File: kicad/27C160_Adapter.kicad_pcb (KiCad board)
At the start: 2 copper layers, 82.4 x 43.1 mm, 10 parts, among them Q1 BC327, SW1 MS22D16, SW2 DIP, U1 27C4002

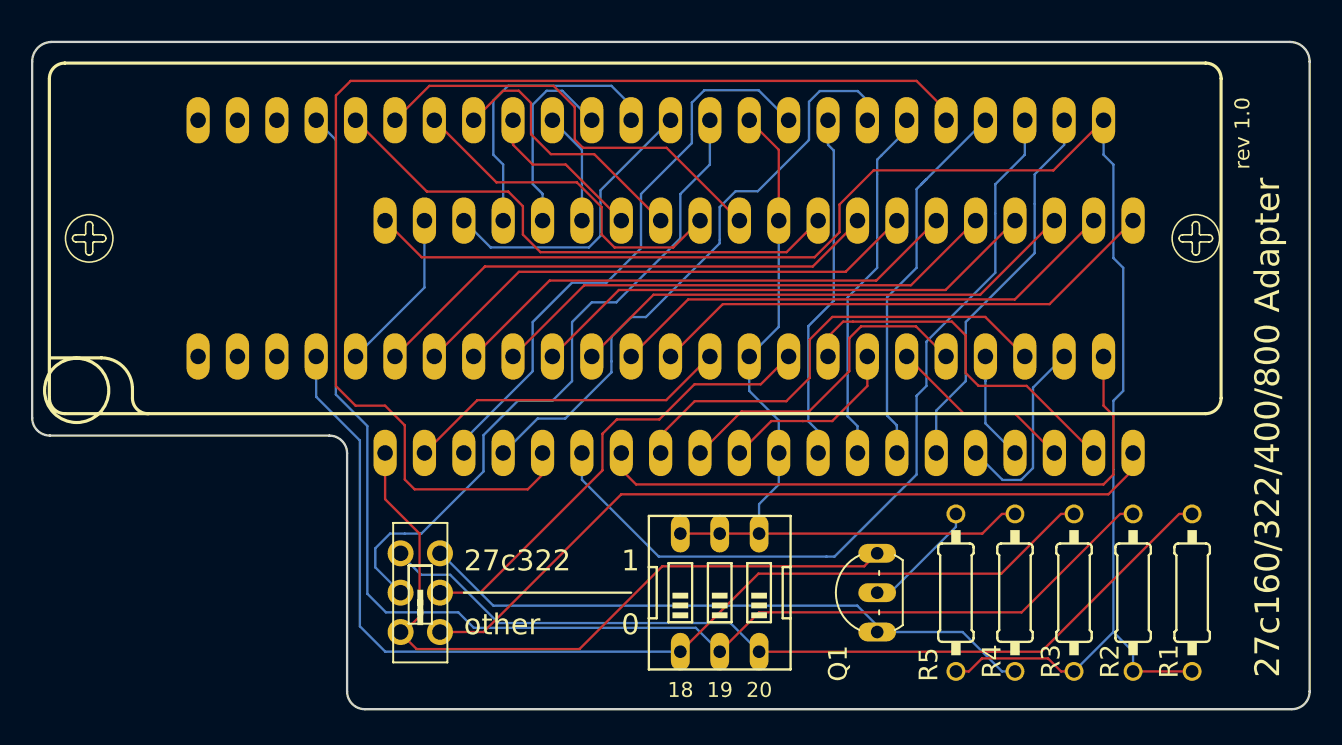
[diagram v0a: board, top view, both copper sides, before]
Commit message: Changed dip switch to coded rotary switch. Still needs rerouting.
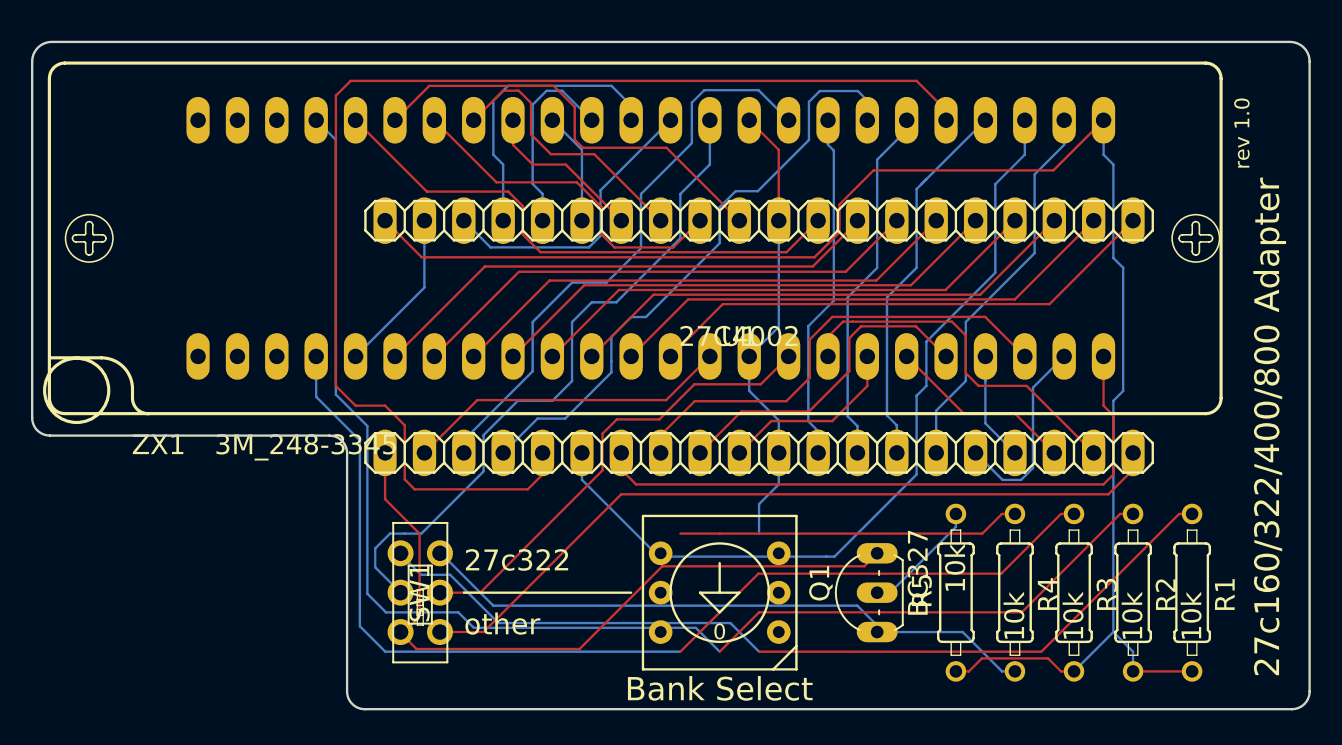
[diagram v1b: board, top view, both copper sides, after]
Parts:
- Q1: footprint TO92-EBC -> 27C160_Adapter:TO92-EBC
- R1, R2, R3, R4, R5: footprint 0207%2f10 -> 27C160_Adapter:0207_10
- SW1: footprint MS22D16 -> 27C160_Adapter:MS22D16
- SW2: value DIP -> 94HBB08T; footprint EDG-03 -> 27C160_Adapter:94HBB08T
- U1: footprint 27C4002 -> 27C160_Adapter:27C4002
- ZX1: footprint 3M_248-3345 -> 27C160_Adapter:3M_248-3345
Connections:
- R1 pad 2: VCC -> GND
- R2 pad 2: VCC -> GND
- R3 pad 2: VCC -> GND
- SW2 pad 1: /A18 -> /A20
- SW2 pad 4: GND -> /A18
- ZX1 pad 1: (no net) -> Net-(ZX1-Pad1)
- ZX1 pad 2: (no net) -> Net-(ZX1-Pad2)
- ZX1 pad 3: (no net) -> Net-(ZX1-Pad3)
- ZX1 pad 46: (no net) -> Net-(ZX1-Pad46)
- ZX1 pad 47: (no net) -> Net-(ZX1-Pad47)
- ZX1 pad 48: (no net) -> Net-(ZX1-Pad48)
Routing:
- net GND: track 51.7 -> 100.0 mm
- net VCC: track 104.6 -> 56.3 mm
- net /A19: track 86.6 -> 131.3 mm
- net /D12: track 53.3 -> 8.55 mm
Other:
- board text added: "Bank Select"
- board text removed: "0"
- board text removed: "1"
- board text removed: "18"
- board text removed: "19"
- board text removed: "20"

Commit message: Version 1.1
Changed dip switch to octal coded rotary switch, changed pullups to
pulldowns to work with octal coded rotary switch, rerouted whole board
and fiddled with silkscreen a bit. Fingers crossed I didn't mess it up.
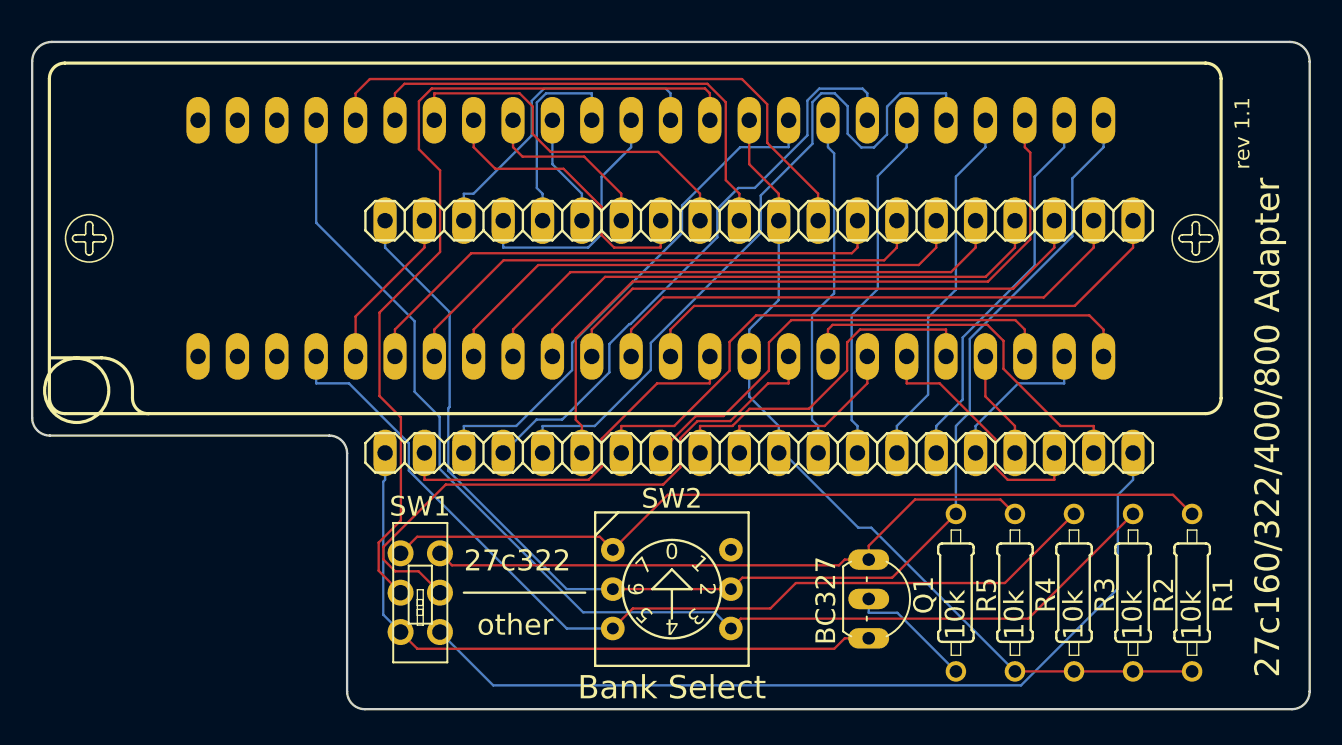
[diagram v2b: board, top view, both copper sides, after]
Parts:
- moved SW2 3.09 mm to (148.6, 118.7), turned to 180 degrees
- moved Q1 2.03 mm to (162.6, 119.4), turned to 270 degrees
- turned R4 to 90 degrees
- turned R5 to 270 degrees
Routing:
- net /A19: track 131.3 -> 77.9 mm
- net GND: track 100.0 -> 56.5 mm
- net /D12: track 8.55 -> 47.4 mm
- net /D13: track 79.9 -> 47.4 mm
- net VCC: track 56.3 -> 85.2 mm
- net /N$2: track 43.5 -> 56.6 mm
- net /N$6: track 30.2 -> 38.7 mm
- net /A18: track 69.0 -> 61.3 mm
- net /N$5: track 50.1 -> 56.9 mm
- net /D1: track 12.1 -> 16.7 mm
- net /E: track 21.0 -> 25.5 mm
- net /VPP: track 46.9 -> 43.0 mm
- net /A9: track 28.0 -> 31.8 mm
- net /A20: track 57.5 -> 53.8 mm
- net /D15: track 37.4 -> 34.0 mm
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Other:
- net class Default: trace_width 0.25 -> 0.1524
- board text added: "0"
- board text added: "1"
- board text added: "2"
- board text added: "3"
- board text added: "4"
- board text added: "5"
- board text added: "6"
- board text added: "7"
- board text added: "original by gaggi modified by DieKatzchen"
- board text added: "rev 1.1"
- board text removed: "by gaggi"
- board text removed: "rev 1.0"
- board text removed: "www.circuit-board.de"

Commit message: Hotfix for LSB error
Whoops! had my LSB and MSB swapped. That would have given some undesired
behavior.
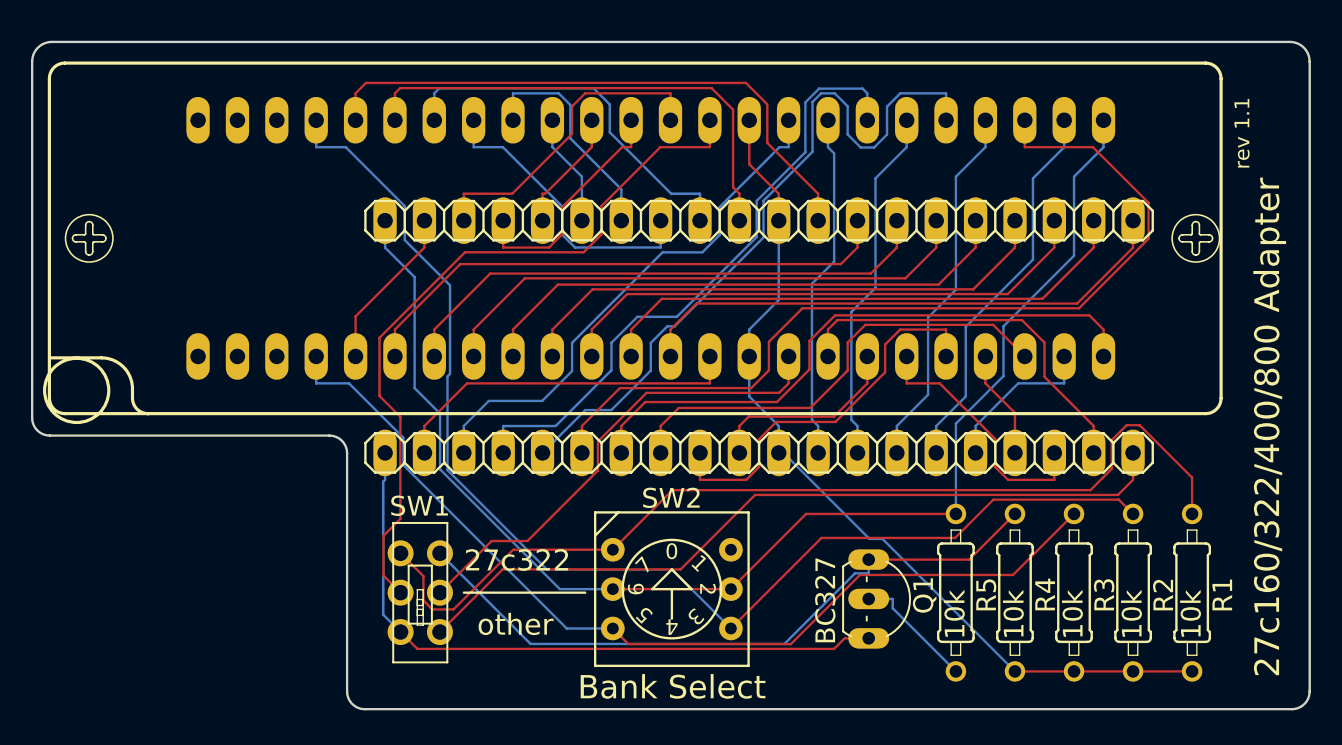
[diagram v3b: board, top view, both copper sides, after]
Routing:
- net /D12: track 47.4 -> 57.9 mm
- net /N$2: track 56.6 -> 47.1 mm
- net /A20: track 53.8 -> 63.2 mm
- net /N$6: track 38.7 -> 30.9 mm
- net /N$5: track 56.9 -> 50.5 mm
- net /A14: track 13.3 -> 7.89 mm
- net /N$4: track 40.1 -> 43.5 mm
- net /A12: track 11.7 -> 14.6 mm
- net /E: track 25.5 -> 23.0 mm
- net /D9: track 23.0 -> 25.5 mm
- net /D14: track 38.6 -> 40.4 mm
- net /A19: track 77.9 -> 79.6 mm
- net /A15: track 16.6 -> 15.4 mm
- net /A18: track 61.3 -> 62.1 mm
- net /D13: track 47.4 -> 46.7 mm
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
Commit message: Actual fix for LSB/MSB mixup
Had actually only rearranged the pulldown resistors. Which doesn't
actually do anything at all. Let this be a lesson: if you make a
correction at 2AM, check it before you send it to the fab house. Fixes
Issue #1 .
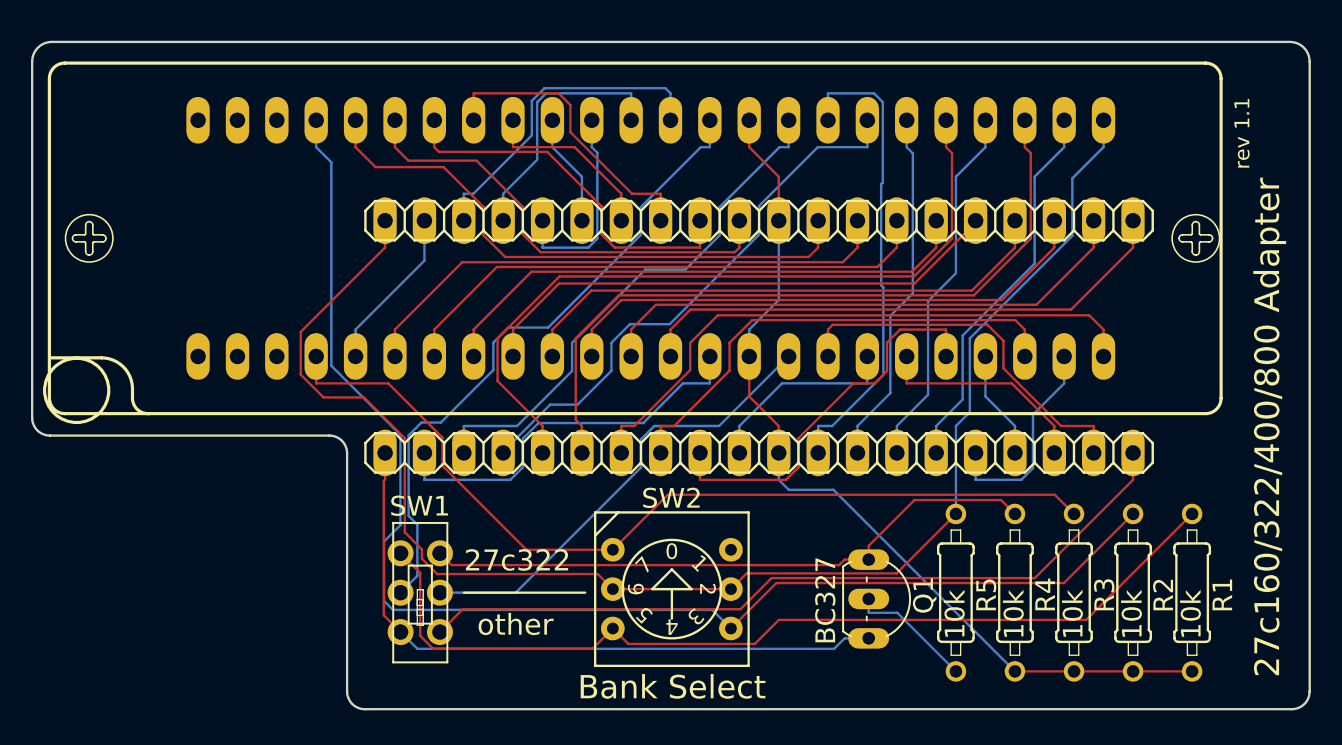
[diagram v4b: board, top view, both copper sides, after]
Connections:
- SW2 pad 1: /A20 -> /A18
- SW2 pad 4: /A18 -> /A20
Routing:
- net /D12: track 57.9 -> 47.4 mm
- net VCC: track 85.4 -> 95.5 mm
- net /D7: track 22.4 -> 30.5 mm
- net /A19: track 79.6 -> 85.8 mm
- net /A14: track 7.89 -> 13.3 mm
- net /N$2: track 47.1 -> 41.8 mm
- net /D14: track 40.4 -> 35.6 mm
- net /A18: track 62.1 -> 58.1 mm
- net /N$4: track 43.5 -> 40.0 mm
- net /D3: track 10.3 -> 13.8 mm
- net /A12: track 14.6 -> 11.7 mm
- net /A20: track 63.2 -> 60.4 mm
- net /E: track 23.0 -> 25.6 mm
- net /D1: track 16.6 -> 14.1 mm
- net /A9: track 31.6 -> 29.7 mm
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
